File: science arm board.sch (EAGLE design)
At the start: 38 parts, among them J4 SL02-HORIZ, J5 SL02-HORIZ, J6 SL03THROUGH_HOLE, U1 OKI-78SR-5/1.5-W36HC, U2 OKI-78SR-5/1.5-W36HC

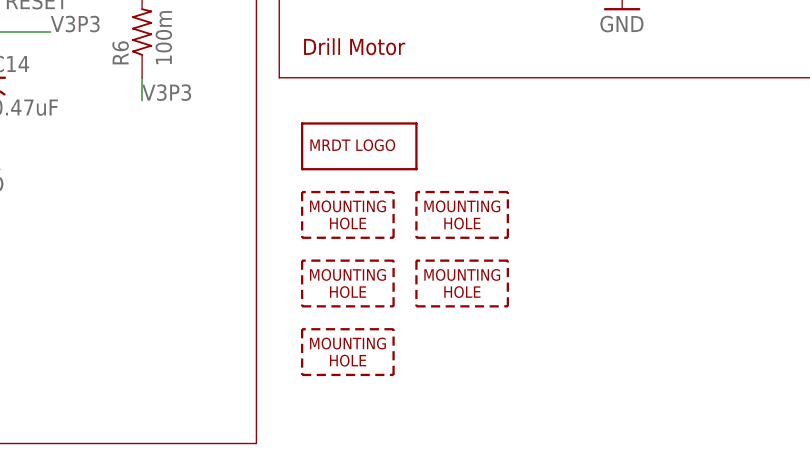
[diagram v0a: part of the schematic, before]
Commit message: Finished routing and labeled board
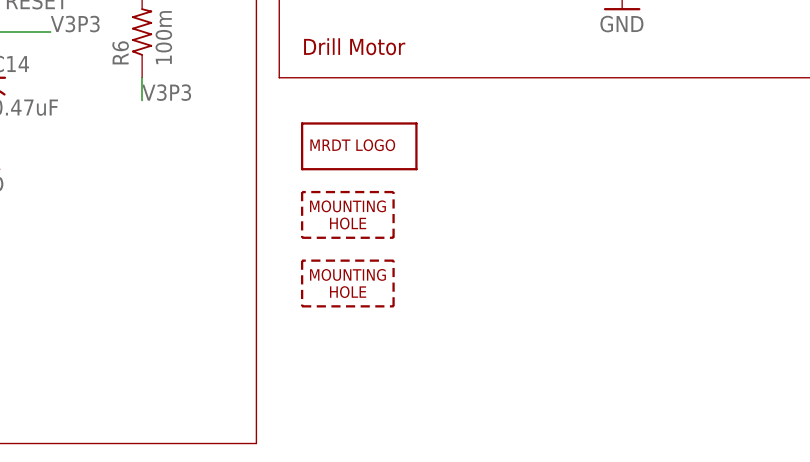
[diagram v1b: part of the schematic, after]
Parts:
- removed H2, H3, H4: MOUNTING_HOLE#6, MRDT-Hardware:MOUNTING_HOLE#6
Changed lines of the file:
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@@
 <part name="LOGO1" library="MRDT-Hardware" deviceset="MRDT_LOGO" device=""/>
 <part name="H1" library="MRDT-Hardware" deviceset="MOUNTING_HOLE" device="#6"/>
-<part name="H2" library="MRDT-Hardware" deviceset="MOUNTING_HOLE" device="#6"/>
-<part name="H3" library="MRDT-Hardware" deviceset="MOUNTING_HOLE" device="#6"/>
-<part name="H4" library="MRDT-Hardware" deviceset="MOUNTING_HOLE" device="#6"/>
 <part name="H5" library="MRDT-Hardware" deviceset="MOUNTING_HOLE" device="#6"/>
 <part name="J6" library="MRDT-Connectors" deviceset="SL03" device="THROUGH_HOLE"/>
@@
 <instance part="LOGO1" gate="G$1" x="7.62" y="-45.72"/>
 <instance part="H1" gate="G$1" x="7.62" y="-53.34"/>
-<instance part="H2" gate="G$1" x="7.62" y="-60.96"/>
-<instance part="H3" gate="G$1" x="7.62" y="-68.58"/>
-<instance part="H4" gate="G$1" x="20.32" y="-53.34"/>
-<instance part="H5" gate="G$1" x="20.32" y="-60.96"/>
+<instance part="H5" gate="G$1" x="7.62" y="-60.96"/>
 <instance part="J6" gate="G$1" x="-99.06" y="40.64" rot="R180"/>
 <instance part="GND16" gate="1" x="-83.82" y="33.02"/>
